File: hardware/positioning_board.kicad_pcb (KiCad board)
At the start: 4 copper layers, 75 x 40 mm, 50 parts, among them J1 Conn_01x04, J2 Conn_01x05, J3 Conn_01x05, J4 4P4C, J5 USB_C_Receptacle_USB2.0_16P, Q1 MMBT3904, Q2 MMBT3904, SW1 SW_Push, SW2 SW_Push, U1 AMS1117-3.3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

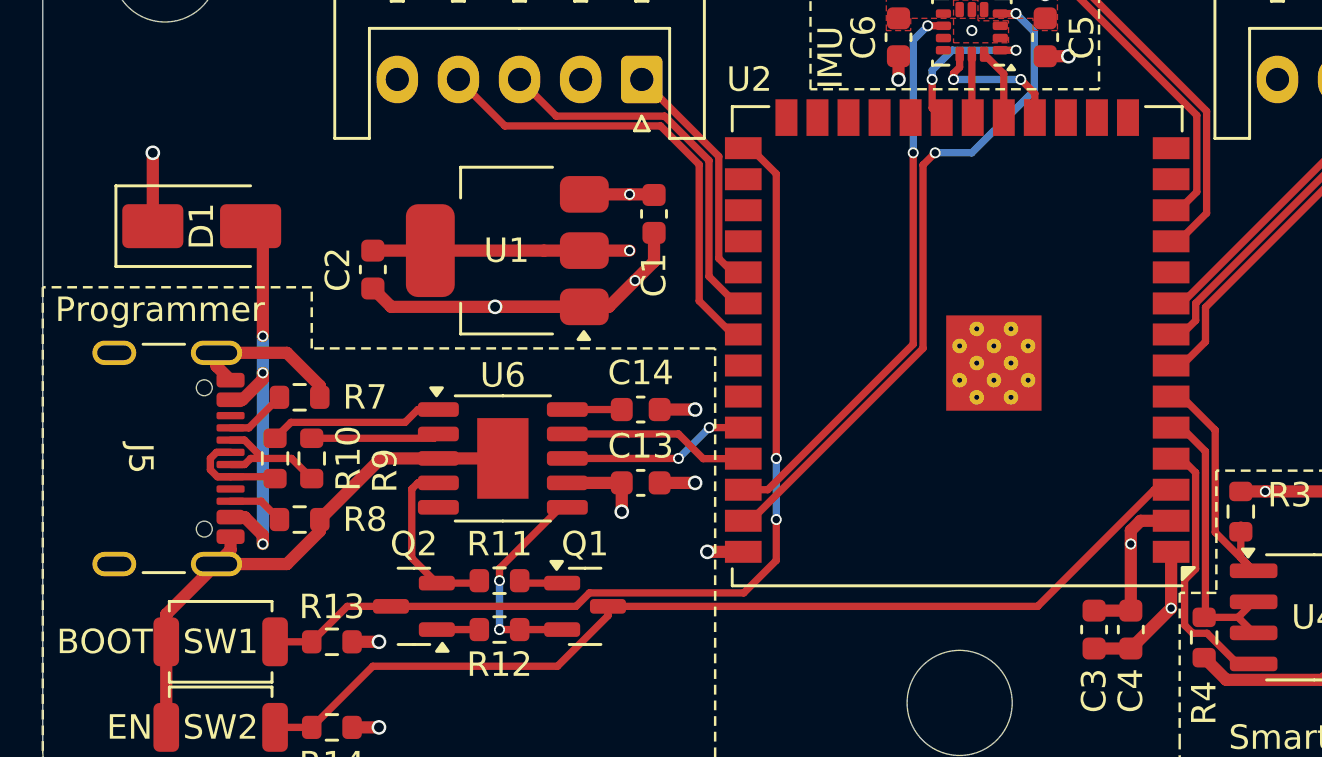
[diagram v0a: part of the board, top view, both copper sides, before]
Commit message: add empty space around holes
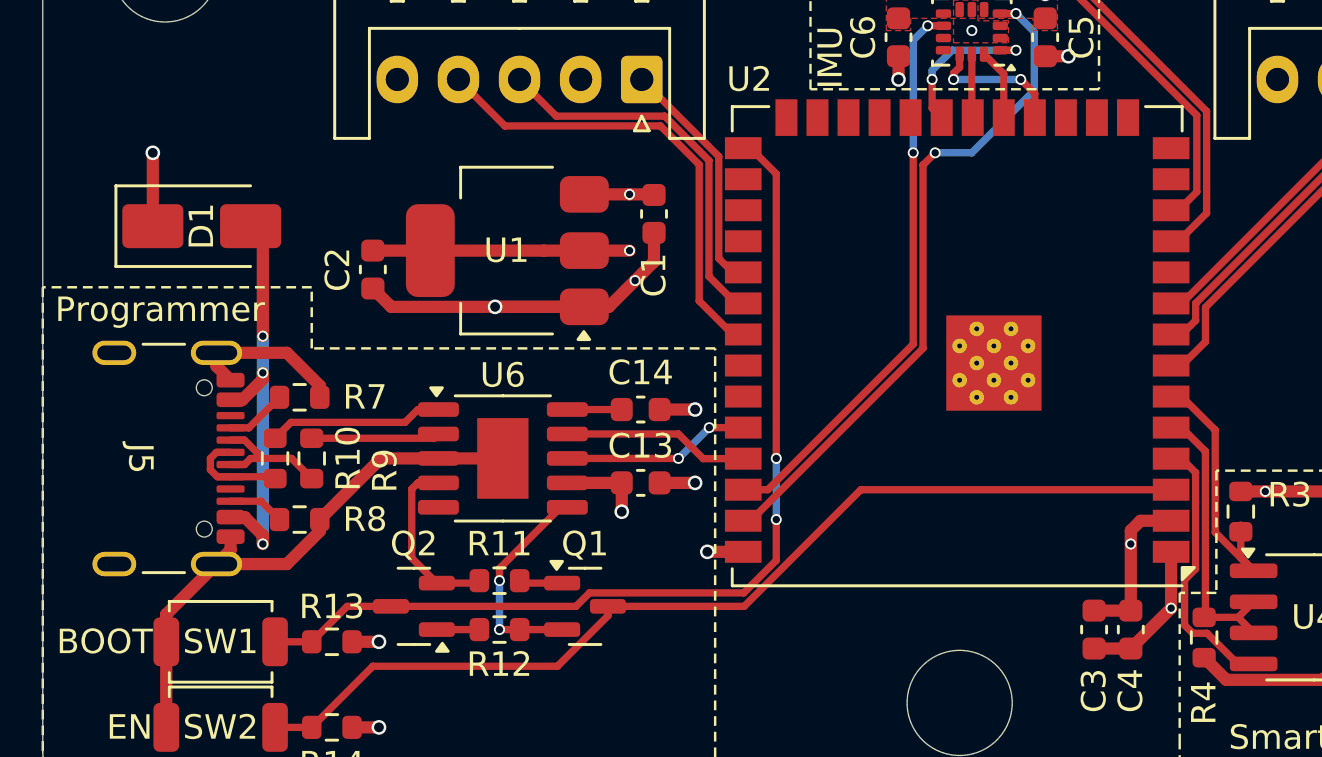
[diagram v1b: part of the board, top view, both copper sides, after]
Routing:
- net +5V: track 7.36 -> 7.86 mm
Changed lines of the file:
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@@
 			(size 4.3 4.3)
 			(drill 4.3)
-			(layers "*.Cu" "*.Mask")
+			(layers "F&B.Cu" "*.Mask")
+			(clearance 2)
 		)
 		(embedded_fonts no)
@@
 			(size 4.3 4.3)
 			(drill 4.3)
-			(layers "*.Cu" "*.Mask")
+			(layers "F&B.Cu" "*.Mask")
+			(clearance 2)
 		)
 		(embedded_fonts no)
@@
 			(size 4.3 4.3)
 			(drill 4.3)
-			(layers "*.Cu" "*.Mask")
+			(layers "F&B.Cu" "*.Mask")
+			(clearance 2)
 		)
 		(embedded_fonts no)
@@
 	)
 	(segment
-		(start 107 85)
+		(start 107 85.5)
 		(end 107 82.5)
 		(width 0.5)
@@
 	)
 	(segment
-		(start 147.96148 96.28)
-		(end 148.65 96.28)
+		(start 125.6175 101.05)
+		(end 131.1891 101.05)
 		(width 0.3)
 		(layer "F.Cu")
@@
 	)
 	(segment
-		(start 125.6175 101.05)
-		(end 143.19148 101.05)
+		(start 131.1891 101.05)
+		(end 135.9591 96.28)
 		(width 0.3)
 		(layer "F.Cu")
@@
 	)
 	(segment
-		(start 143.19148 101.05)
-		(end 147.96148 96.28)
+		(start 135.9591 96.28)
+		(end 136 96.28)
 		(width 0.3)
 		(layer "F.Cu")
@@
 		(width 0.3)
 		(layer "F.Cu")
+		(net 22)
+	)
+	(segment
+		(start 136 96.28)
+		(end 148.65 96.28)
+		(width 0.3)
+		(layer "F.Cu")

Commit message: fix: remove traces from underneath IMU
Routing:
- net +3V3: track 30.5 -> 37.4 mm, vias 7 -> 8
- net GND: track 74.3 -> 78.3 mm
- removed copper zone on F.Cu, net +3V3
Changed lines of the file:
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@@
+	)
+	(segment
+		(start 137.5 77)
+		(end 137.5 76)
+		(width 0.3)
+		(layer "F.Cu")
+		(net 11)
 	)
 	(segment
@@
 	)
 	(segment
+		(start 141 76.6425)
+		(end 141.6425 76)
+		(width 0.3)
+		(layer "F.Cu")
+		(net 11)
+	)
+	(segment
 		(start 123.955 96)
 		(end 126.18 96)
@@
 	)
 	(segment
+		(start 143.5 77)
+		(end 143.5 76)
+		(width 0.3)
+		(layer "F.Cu")
+		(net 11)
+	)
+	(segment
 		(start 145.5 101.225)
 		(end 147 101.225)
@@
 	)
 	(segment
+		(start 137.5 76)
+		(end 138.5325 76)
+		(width 0.3)
+		(layer "F.Cu")
+		(net 11)
+	)
+	(segment
 		(start 116 86.5)
 		(end 118.35 86.5)
@@
 	)
 	(segment
+		(start 138.5325 76)
+		(end 139.3375 76.805)
+		(width 0.3)
+		(layer "F.Cu")
+		(net 11)
+	)
+	(segment
 		(start 147.4 97.55)
 		(end 148.65 97.55)
@@
 		(end 152.5 96.35)
 		(width 0.5)
+		(layer "F.Cu")
+		(net 11)
+	)
+	(segment
+		(start 141.6425 76)
+		(end 143.5 76)
+		(width 0.3)
 		(layer "F.Cu")
 		(net 11)
@@
 	)
 	(via
+		(at 137.5 76)
+		(size 0.6)
+		(drill 0.4)
+		(layers "F.Cu" "B.Cu")
+		(net 11)
+	)
+	(via
 		(at 126.5 86.5)
 		(size 0.45)
@@
 		(layers "F.Cu" "B.Cu")
 		(net 11)
+	)
+	(segment
+		(start 141.6625 77.305)
+		(end 141.6625 77.805)
+		(width 0.3)
+		(layer "F.Cu")
+		(net 12)
 	)
 	(segment
@@
 	)
 	(segment
+		(start 140 76.6425)
+		(end 140 76)
+		(width 0.3)
+		(layer "F.Cu")
+		(net 12)
+	)
+	(segment
 		(start 155.5 103.405)
 		(end 156.975 103.405)
@@
 	)
 	(segment
+		(start 141.6625 77.305)
+		(end 142.1115 77.754)
+		(width 0.3)
+		(layer "F.Cu")
+		(net 12)
+	)
+	(segment
 		(start 127.5 86.95)
 		(end 126.725 87.725)
@@
 	)
 	(segment
+		(start 140 76.6425)
+		(end 140.5 76.6425)
+		(width 0.3)
+		(layer "F.Cu")
+		(net 12)
+	)
+	(segment
 		(start 113.83 92.025)
 		(end 113.83 92.5)
@@
 	)
 	(segment
+		(start 142.704 77.754)
+		(end 143.5 78.55)
+		(width 0.3)
+		(layer "F.Cu")
+		(net 12)
+	)
+	(segment
 		(start 109.605 91.225)
 		(end 110.18 91.8)
@@
 		(end 124.65 88.8)
 		(width 0.5)
+		(layer "F.Cu")
+		(net 12)
+	)
+	(segment
+		(start 142.1115 77.754)
+		(end 142.704 77.754)
+		(width 0.3)
 		(layer "F.Cu")
 		(net 12)
@@
 	)
 	(via
+		(at 140 76)
+		(size 0.6)
+		(drill 0.4)
+		(layers "F.Cu" "B.Cu")
+		(net 12)
+	)
+	(via
 		(at 160.5 101.5)
 		(size 0.6)
@@
 	(via
 		(at 170.5 88.5)
-		(size 0.45)
-		(drill 0.3)
-		(layers "F.Cu" "B.Cu")
-		(free yes)
-		(net 12)
-	)
-	(via
-		(at 140.5 77.5)
 		(size 0.45)
 		(drill 0.3)
@@
 			(pts
 				(xy 172 85) (xy 167.5 85) (xy 167.5 86.5) (xy 157.5 86.5) (xy 157.5 83) (xy 172 83)
-			)
-		)
-	)
-	(zone
-		(net 12)
-		(net_name "GND")
-		(layer "F.Cu")
-		(hatch edge 0.5)
-		(priority 1)
-		(connect_pads yes
-			(clearance 0.1)
-		)
-		(min_thickness 0.25)
-		(filled_areas_thickness no)
-		(fill yes
-			(thermal_gap 0.5)
-			(thermal_bridge_width 0.5)
-			(smoothing fillet)
-			(radius 0.5)
-		)
-		(polygon
-			(pts
-				(xy 139.75 76.25) (xy 139.75 78) (xy 142 78) (xy 142 77.1) (xy 140.75 77.1) (xy 140.75 76.25)
 			)
 		)
@@
 			)
 		)
-	)
-	(zone
-		(net 11)
-		(net_name "+3V3")
-		(layer "F.Cu")
-		(hatch edge 0.5)
-		(priority 1)
-		(connect_pads yes
-			(clearance 0.1)
-		)
-		(min_thickness 0.25)
-		(filled_areas_thickness no)
-		(fill yes
-			(thermal_gap 0.5)
-			(thermal_bridge_width 0.5)
-			(smoothing fillet)
-			(radius 0.5)
-		)
-		(polygon
-			(pts
-				(xy 137 77.5) (xy 137 75.25) (xy 144 75.25) (xy 144 77.5) (xy 143 77.5) (xy 143 77) (xy 138 77)
-				(xy 138 77.5)
-			)
-		)

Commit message: add back labels
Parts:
- added G***: LOGO, LOGO, B.Cu at (130.0, 103.0)
- added G***: LOGO, LOGO, B.Cu at (156.0, 91.0)
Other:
- board text added: "+5V"
- board text added: "5V"
- board text added: "A"
- board text added: "B"
- board text added: "Design by Ashie"
- board text added: "Encoder 1"
- board text added: "Encoder 2"
- board text added: "GND"
- board text added: "LIDAR"
- board text added: "PWM"
- board text added: "Positioning System"
- board text added: "RX"
- board text added: "The robot knows where it is at all times. It knows this because it knows where it isn't."
- board text added: "X"

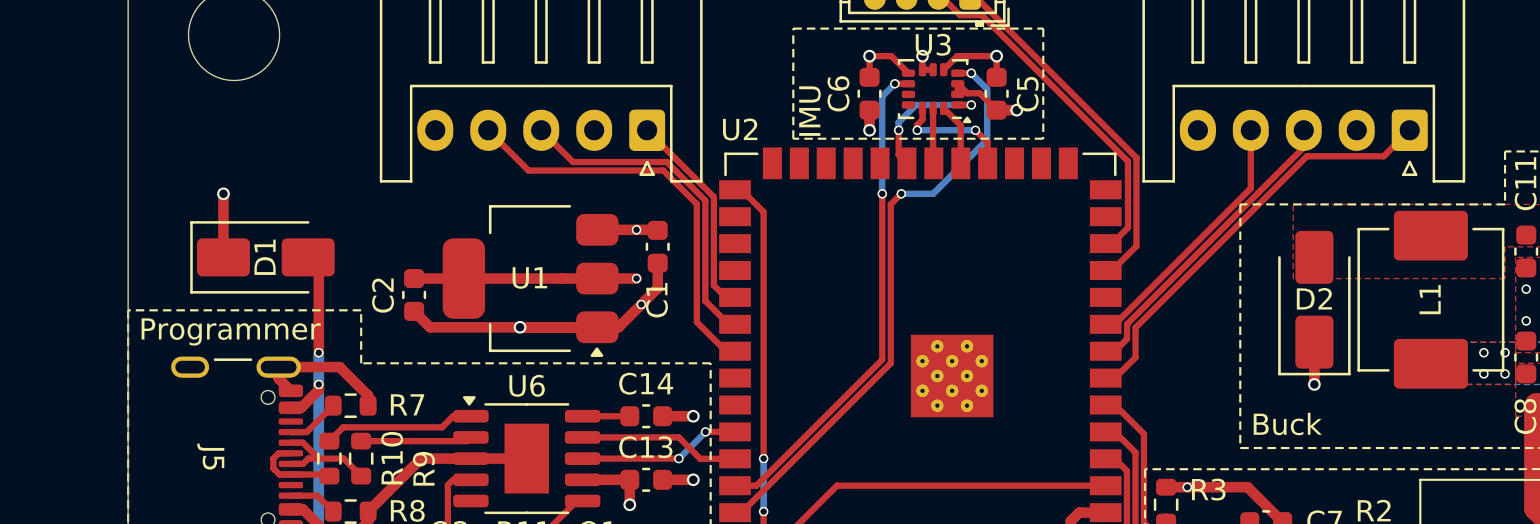
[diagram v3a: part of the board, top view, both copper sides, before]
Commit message: add logic level shifters
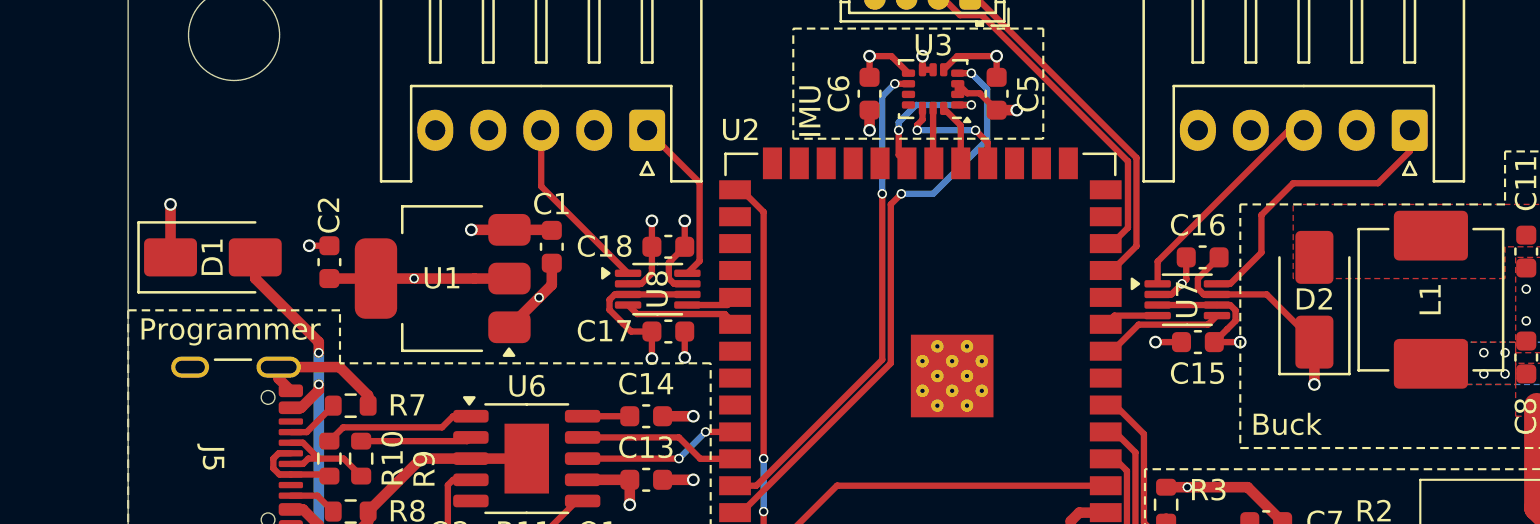
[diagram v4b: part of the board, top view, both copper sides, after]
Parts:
- added C15: 100n, Capacitor_SMD:C_0603_1608Metric, F.Cu at (153.0, 89.5)
- added C16: 100n, Capacitor_SMD:C_0603_1608Metric, F.Cu at (153.2, 85.5)
- added C17: 100n, Capacitor_SMD:C_0603_1608Metric, F.Cu at (128.0, 89.0)
- added C18: 100n, Capacitor_SMD:C_0603_1608Metric, F.Cu at (128.0, 85.0)
- added U7: TXB0102DCU, Package_SO:VSSOP-8_2.3x2mm_P0.5mm, F.Cu at (152.5, 87.5)
- added U8: TXB0102DCU, Package_SO:VSSOP-8_2.3x2mm_P0.5mm, F.Cu at (127.5, 87.0)
- moved C1 5.00 mm to (122.5, 85.0)
- moved C2 4.29 mm to (112.0, 85.7), turned to -90 degrees
- moved U1 4.15 mm to (117.3, 86.5)
- moved D1 2.50 mm to (106.5, 85.5)
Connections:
- J2 pad 1: /Encoder1_B -> Net-(J2-Pin_1)
- J2 pad 3: /Encoder1_A -> Net-(J2-Pin_3)
- J2 pad 4: /Encoder1_X -> unconnected-(J2-Pin_4-Pad4)
- J3 pad 1: /Encoder2_B -> Net-(J3-Pin_1)
- J3 pad 3: /Encoder2_A -> Net-(J3-Pin_3)
- J3 pad 4: /Encoder2_X -> unconnected-(J3-Pin_4-Pad4)
- U2 pad 33: /Encoder2_X -> unconnected-(U2-IO40-Pad33)
- U2 pad 7: /Encoder1_B -> unconnected-(U2-IO7-Pad7)
- U2 pad 8: /Encoder1_A -> /Encoder1_B
- U2 pad 9: /Encoder1_X -> /Encoder1_A
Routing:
- net /Encoder2_X: track 19.2 -> 0.00 mm
- net /Encoder1_B: track 20.0 -> 5.95 mm
- net Net-(J2-Pin_1): track 0.00 -> 13.7 mm
- net +5V: track 7.86 -> 20.8 mm, vias 3 -> 4
- net +3V3: track 37.4 -> 50.3 mm, vias 8 -> 10
- net /Encoder1_X: track 12.3 -> 0.00 mm
- net /Encoder1_A: track 14.6 -> 2.62 mm
- net Net-(J2-Pin_3): track 0.00 -> 10.5 mm
- net /Encoder2_A: track 15.7 -> 5.43 mm
- net Net-(J3-Pin_3): track 0.00 -> 8.45 mm
- net Net-(J3-Pin_1): track 0.00 -> 8.01 mm
- net /Encoder2_B: track 9.86 -> 2.40 mm
- net GND: track 78.3 -> 74.7 mm, vias 18 -> 22
- net /usb_port/+5V: track 17.1 -> 18.2 mm
